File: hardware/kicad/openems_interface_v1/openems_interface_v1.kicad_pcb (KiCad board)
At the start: 2 copper layers, 130 x 100 mm, 20 parts, among them J1 rusEFI_AMPSEAL_35_RA_776180, J2 TE_770669_AMPSEAL_23_RA, J3 WeAct_PinHeader_2x25_P2.54mm, J4 WeAct_PinHeader_2x25_P2.54mm, Q1 SOT-23, U1 SOT-23-6, U2 SOT-23-5, U3 LQFP-100_14x14mm_P0.5mm

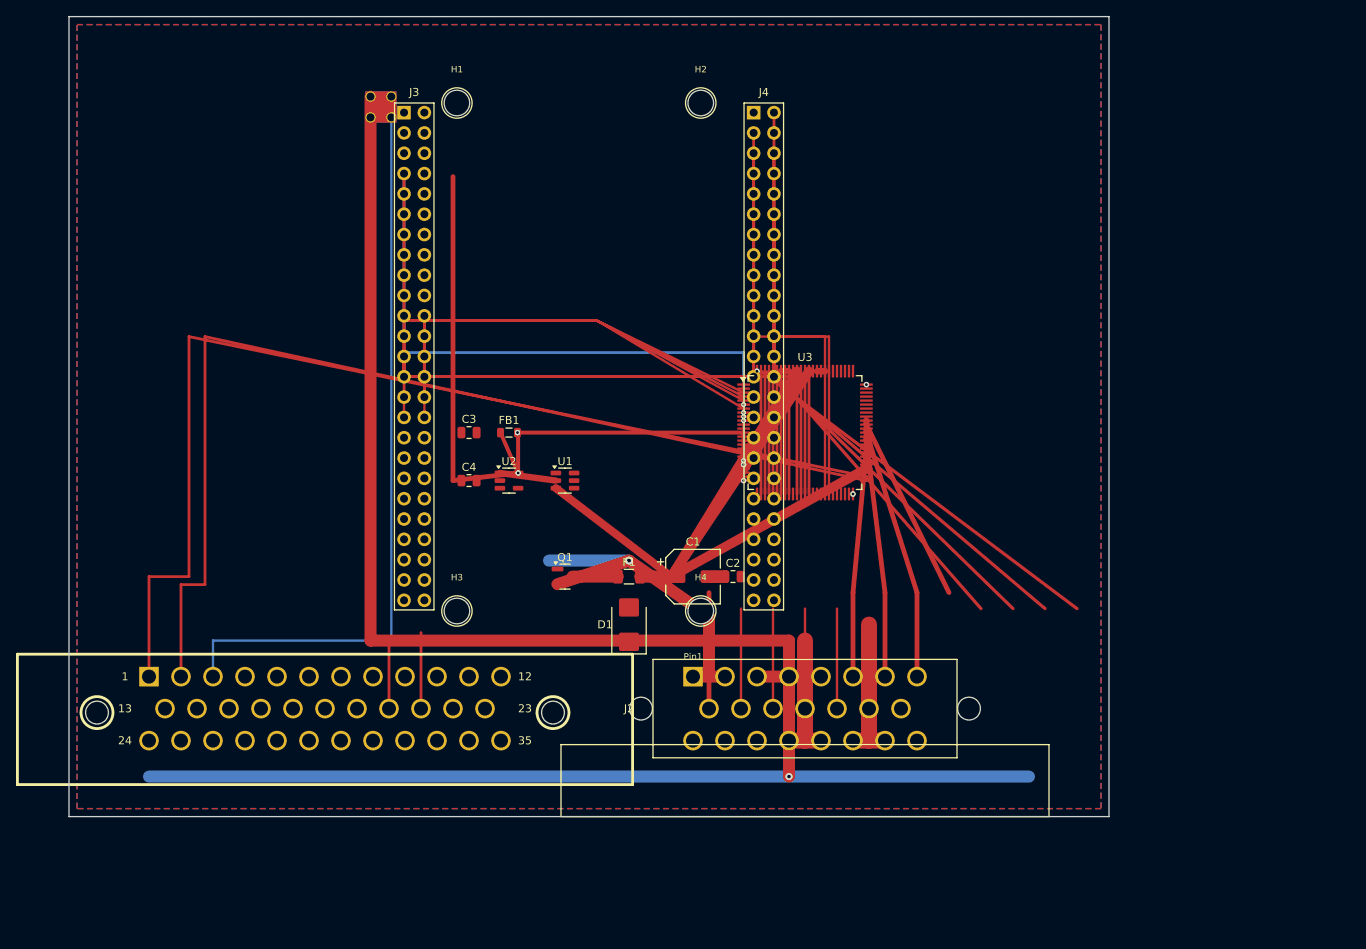
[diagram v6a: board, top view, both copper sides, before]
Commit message: fix(hw): PCB layout limpo — placement + bridges locais só
Substitui o auto-route emaranhado (~127 segs) por layout_clean.py:
zonas claras, ~22 segs (pares J2, A+B TLE, cadeia power). Routing
fino fica para o Pcbnew à mão.
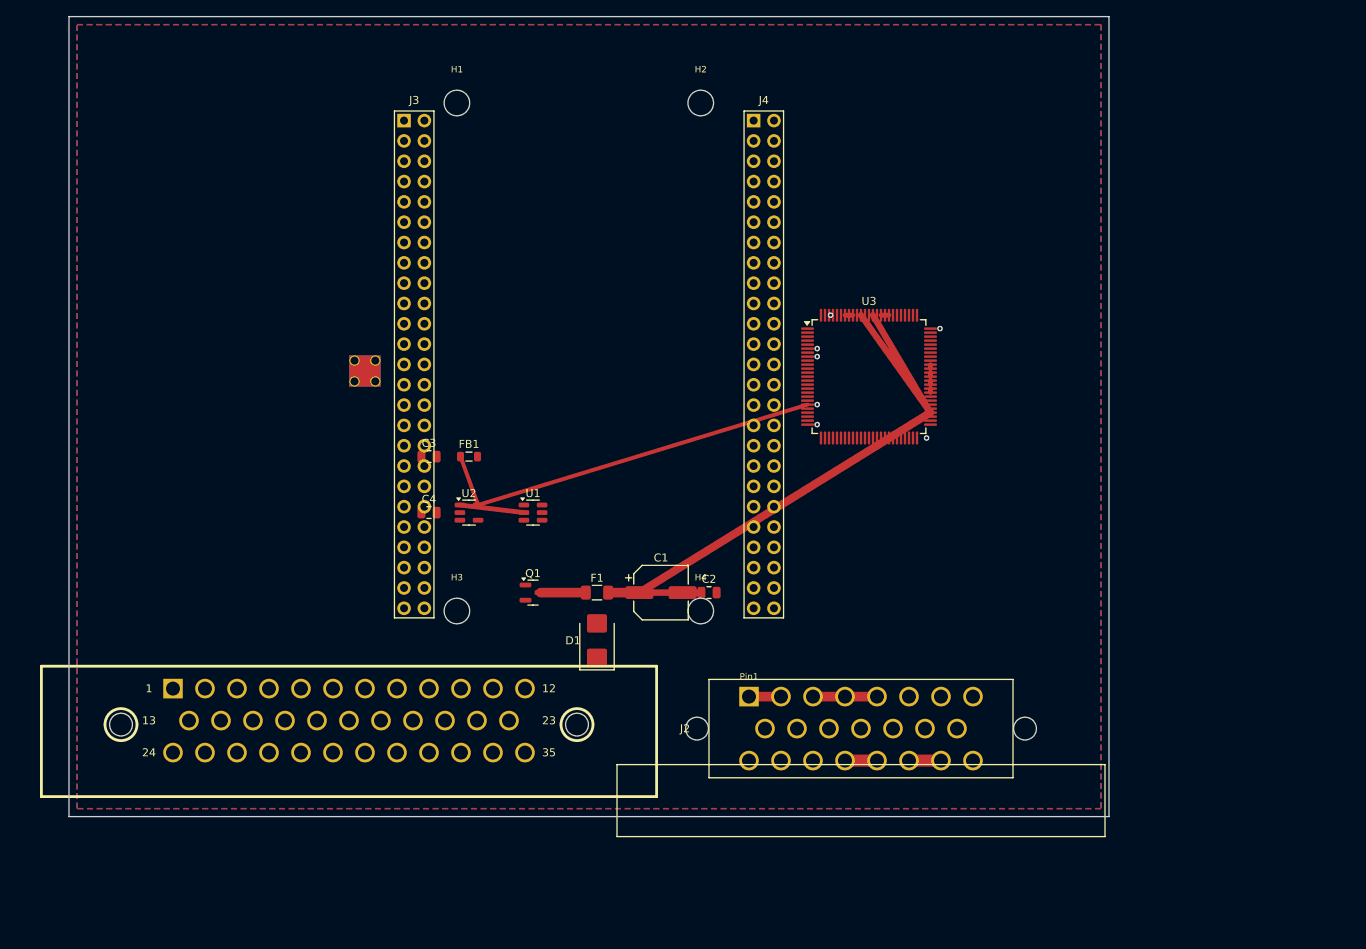
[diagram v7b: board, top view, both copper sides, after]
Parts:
- H1, H2, H3, H4: value MH3.2 -> MH
- J1: value rusEFI_AMPSEAL_35_RA_776180 -> 776180
- moved NT1 33.1 mm to (35.7, 43.0)
- moved U3 10.6 mm to (100.0, 45.0)
- moved J2 7.43 mm to (85.0, 85.0)
- moved C4 6.40 mm to (45.0, 62.0)
- moved U2 6.40 mm to (50.0, 62.0)
- moved C3 5.83 mm to (45.0, 55.0)
- moved FB1 5.83 mm to (50.0, 55.0)
- moved U1 5.66 mm to (58.0, 62.0)
- moved C1 4.47 mm to (74.0, 72.0)
- moved D1 4.47 mm to (66.0, 78.0)
- moved F1 4.47 mm to (66.0, 72.0)
- moved Q1 4.47 mm to (58.0, 72.0)
- moved C2 3.61 mm to (80.0, 72.0)
- moved J1 3.35 mm to (35.0, 88.0)
- moved J3 1.00 mm to (43.1, 13.0)
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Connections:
- J4 pad 1: VB_WEACT -> (no net)
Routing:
- net PGND: track 255.3 -> 8.00 mm, vias 5 -> 3
- net MCU_PA0: track 157.7 -> 0.00 mm, vias 1 -> 0
- net CKP_P: track 134.0 -> 0.00 mm
- net CKP_N: track 130.1 -> 0.00 mm
- net SHIELD_GND: track 92.2 -> 0.00 mm, vias 1 -> 0
- net MCU_PE10: track 68.9 -> 0.00 mm
- net MCU_PE9: track 66.9 -> 0.00 mm
- net MCU_PE12: track 66.8 -> 0.00 mm
- net MCU_PE11: track 64.8 -> 0.00 mm
- net MCU_PE13: track 62.8 -> 0.00 mm
- net IGN4: track 61.9 -> 0.00 mm
- net IGN3: track 58.4 -> 0.00 mm
- net MCU_PB14: track 56.9 -> 0.00 mm
- net IGN2: track 55.1 -> 0.00 mm
- net MCU_PB15: track 54.6 -> 0.00 mm
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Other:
- board text added: "CLEAN LAYOUT — only local bridges + PGND pours Route remaining nets by hand in Pcbnew Edit → Fill All Zones | Inspect → DRC NAO fabricar sem revisao pin1 / FET / DRC"
- board text added: "J1 AMPSEAL 35 (signals)"
- board text added: "J2 AMPSEAL 23 (power)"
- board text added: "NT1 star GND"
- board text added: "POWER Q1 F1 C bulk buck + LDO"
- board text added: "U3 TLE8888"
- board text added: "WeAct H562 keepout"
- board text removed: "CKP quiet no INJ/ETB"
- board text removed: "Finish: LDO U2 + FB1 VDDA; WeAct J3/J4 nets; SPI/CAN/drive Confirm WeAct pin1 silk vs SchDoc before fab. Not production-ready."
- board text removed: "J1 signals 1-776180-1"
- board text removed: "J2 power 1-770669-1"
- board text removed: "OpenEMS interface v1 — 130x100 mm\nBottom: J1 35 + J2 23 AMPSEAL RA\nCenter: WeAct 38.62x69.10 + MH Phi3.2\nNAO fabricar sem copper/GND pours"
- board text removed: "PGND zones F+B (B: Fill All Zones in Pcbnew) J1/J2 nets = pinmap_logical.md (authoritative) Star NetTie: PGND-SGND-AGND-SHIELD near WeAct AGND pour island near ADC later"
- board text removed: "PWR bay FET/fuse/bulk"
- board text removed: "Power stage: Q1→F1→VBAT bulk→TLE BAT; buck→+5V_MAIN TLE U3 LQFP100 @ (92,52). Straps SIN=AGND FCLN=+3V3 on copper."
- board text removed: "Routing: VBAT_RAW/PGND thick; ETB dual; CKP pair N; SPI keepout Fill zones after open. TLE/power parts not placed yet — stubs only."
- board text removed: "SPI2 corridor PB12-15 ↔ TLE"
- board text removed: "TLE power zone (BAT/OUT stubs)"
- board text removed: "WeAct keepout"

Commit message: fix(hw): floorplan 160x110 sem overlaps nem spaghetti
Placa maior; WeAct top-left, power mid, TLE right, AMPSEAL bottom;
zero overlaps entre componentes; 22 bridges locais apenas.
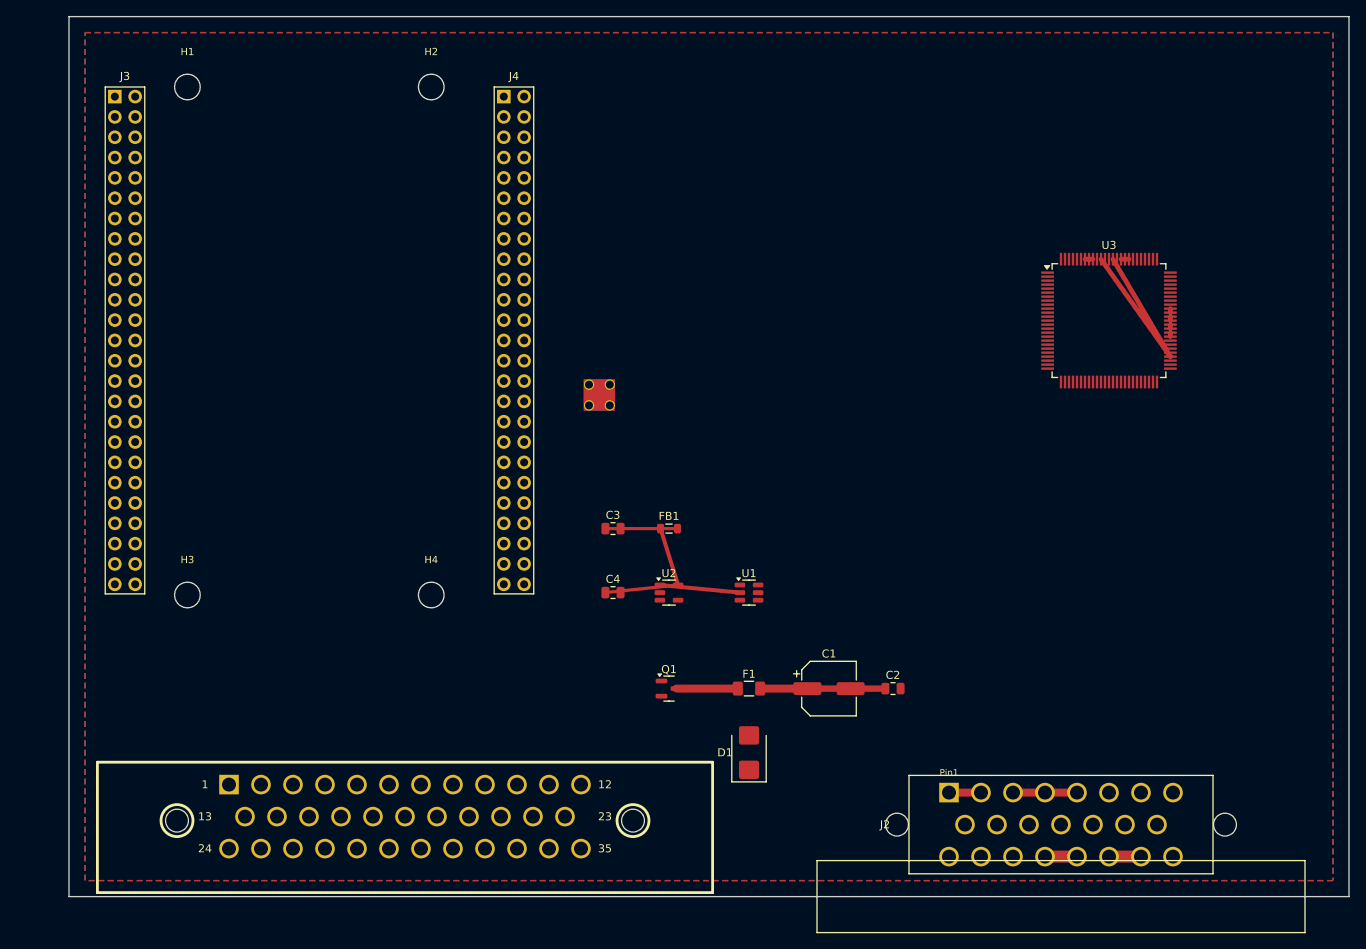
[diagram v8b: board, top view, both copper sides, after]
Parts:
- H1, H2, H3, H4: value MH -> M3
- moved J3 36.3 mm to (7.00, 10.0)
- moved H1 33.7 mm to (14.8, 8.80)
- moved H2 33.7 mm to (45.3, 8.80)
- moved H3 33.7 mm to (14.8, 72.3)
- moved H4 33.7 mm to (45.3, 72.3)
- moved J4 31.4 mm to (55.6, 10.0)
- moved U3 30.8 mm to (130.0, 38.0)
- moved NT1 29.5 mm to (65.0, 46.0)
- moved U1 28.8 mm to (85.0, 72.0)
- moved J2 27.7 mm to (110.0, 97.0)
- moved U2 26.9 mm to (75.0, 72.0)
- moved FB1 26.6 mm to (75.0, 64.0)
- moved C2 25.9 mm to (103.0, 84.0)
- moved C4 25.1 mm to (68.0, 72.0)
- moved C3 24.7 mm to (68.0, 64.0)
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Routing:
- net VBAT: track 89.2 -> 52.4 mm
- net +3V3: track 49.5 -> 16.5 mm, vias 2 -> 0
- net VDDA: track 0.00 -> 9.01 mm
- net +5V_MAIN: track 8.06 -> 10.0 mm
- net PGND: vias 3 -> 0
- net AGND: vias 2 -> 0
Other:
- board size 130 x 100 mm -> 160 x 110 mm
- board text added: "J1 35-pos signals (rusEFI AMPSEAL RA)"
- board text added: "J2 23-pos power (TE 770669 RA)"
- board text added: "LAYOUT LIMPO 160x110 mm So bridges locais (sem auto-route) Home = zoom | Edit > Fill All Zones Roteie o resto a mao | NAO fabricar ainda"
- board text added: "NT1 star"
- board text added: "POWER CHAIN"
- board text added: "U3 TLE8888 LQFP-100"
- board text added: "WeAct H562 38.6 x 69.1"
- board text removed: "CLEAN LAYOUT — only local bridges + PGND pours Route remaining nets by hand in Pcbnew Edit → Fill All Zones | Inspect → DRC NAO fabricar sem revisao pin1 / FET / DRC"
- board text removed: "J1 AMPSEAL 35 (signals)"
- board text removed: "J2 AMPSEAL 23 (power)"
- board text removed: "NT1 star GND"
- board text removed: "POWER Q1 F1 C bulk buck + LDO"
- board text removed: "U3 TLE8888"
- board text removed: "WeAct H562 keepout"
